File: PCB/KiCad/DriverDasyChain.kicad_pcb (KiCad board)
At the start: 4 copper layers, 66.8 x 64 mm, 52 parts, among them J1 Conn_01x03, J10 Conn_01x04, J12 Conn_01x04, J2 Conn_01x03, J3 Conn_01x03, J4 Conn_01x04, J5 Conn_01x03, J6 Conn_01x04, Q2 IRLR3410TRPBF, SW1 SW_DIP_x02, SW2 SW_SPDT, U1 AP2112K-3.3, U2 XIAO-ESP32-S3-DIP, U3 74AHCT1G125, U4 SN65HVD230

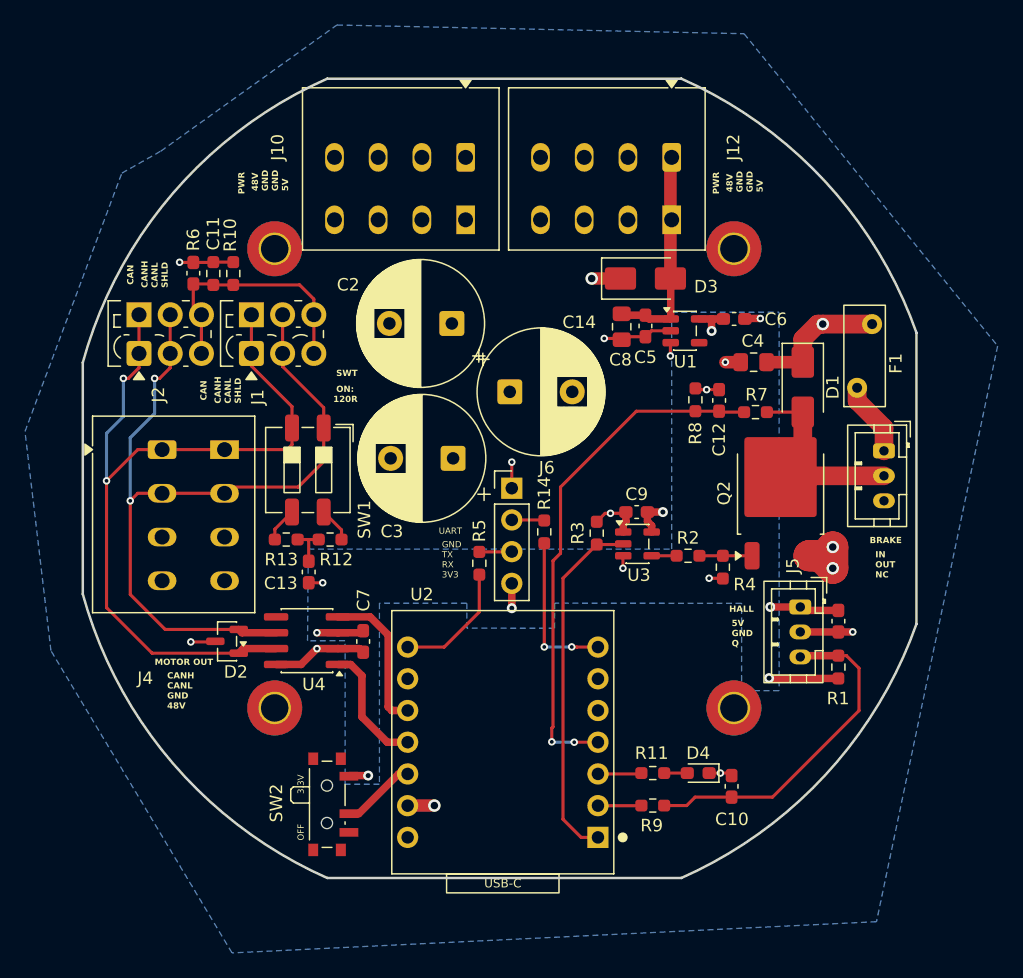
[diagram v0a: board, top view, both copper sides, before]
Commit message: Update PCB daisy chain documentation and layout details
- Enhanced power distribution details for the daisy chain, including updated capacitor specifications for bulk capacitance.
- Clarified the layout topology for the braking circuit and updated the placement of the flyback diode.
- Added a CAN-TVS protection component to the schematic and layout, ensuring proper placement for transceiver protection.
- Verified and documented layout standards, including ground and power plane considerations, and ensured compliance with IPC-2221 standards.
- Updated the status of various tasks related to the PCB design, including completion of split-termination and CAN-TVS integration.
- Added a lock file for the KiCad PCB project to track user access.
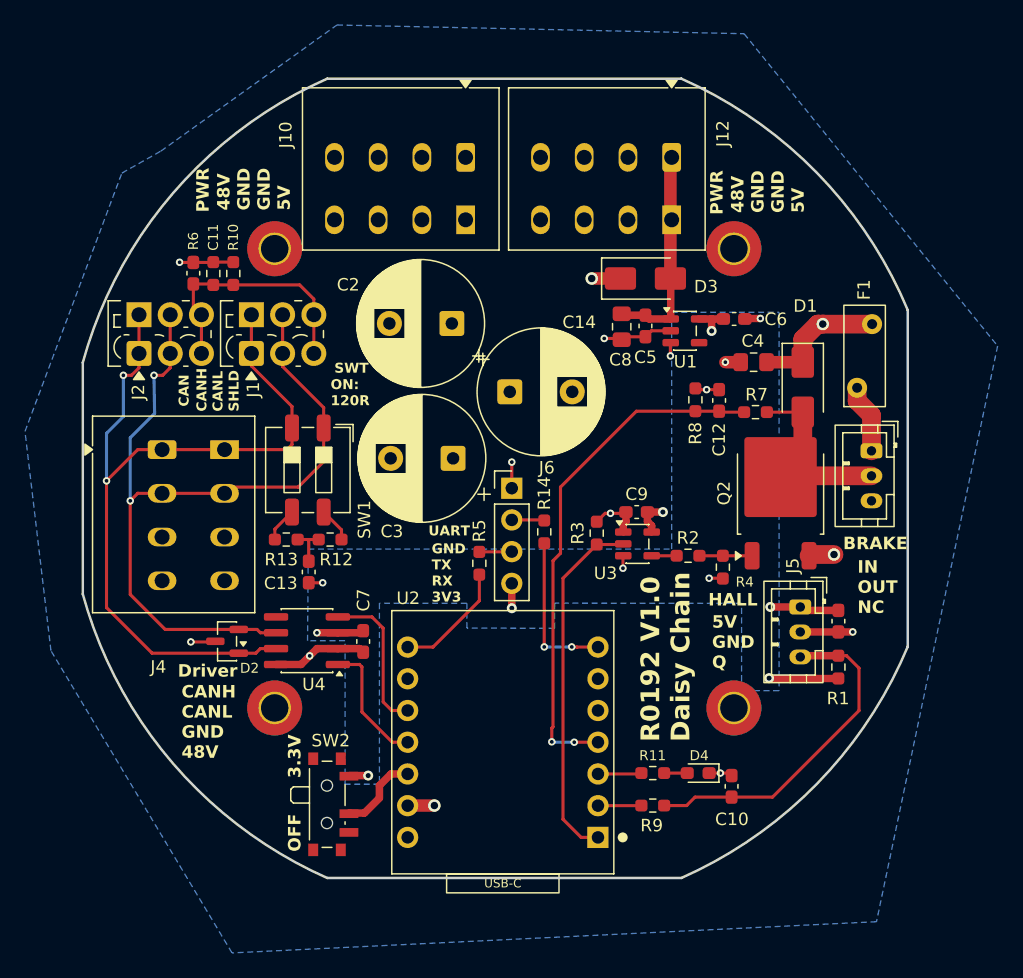
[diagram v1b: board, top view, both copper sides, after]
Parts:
- moved J3 1.00 mm to (179.4, 97.8)
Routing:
- net GND: track 51.1 -> 46.9 mm, vias 18 -> 17
- net /BRAKE Out: track 17.1 -> 16.1 mm
- net Net-(SW2-B): track 6.02 -> 6.60 mm
- net /GPIO D7 (XIAO-ESP32-S3): track 9.89 -> 9.36 mm
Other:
- board size 66.8 x 64 mm -> 66.1 x 64 mm
- board text added: "Driver"
- board text added: "R0192 V1.0 Daisy Chain"
- board text removed: "MOTOR OUT"

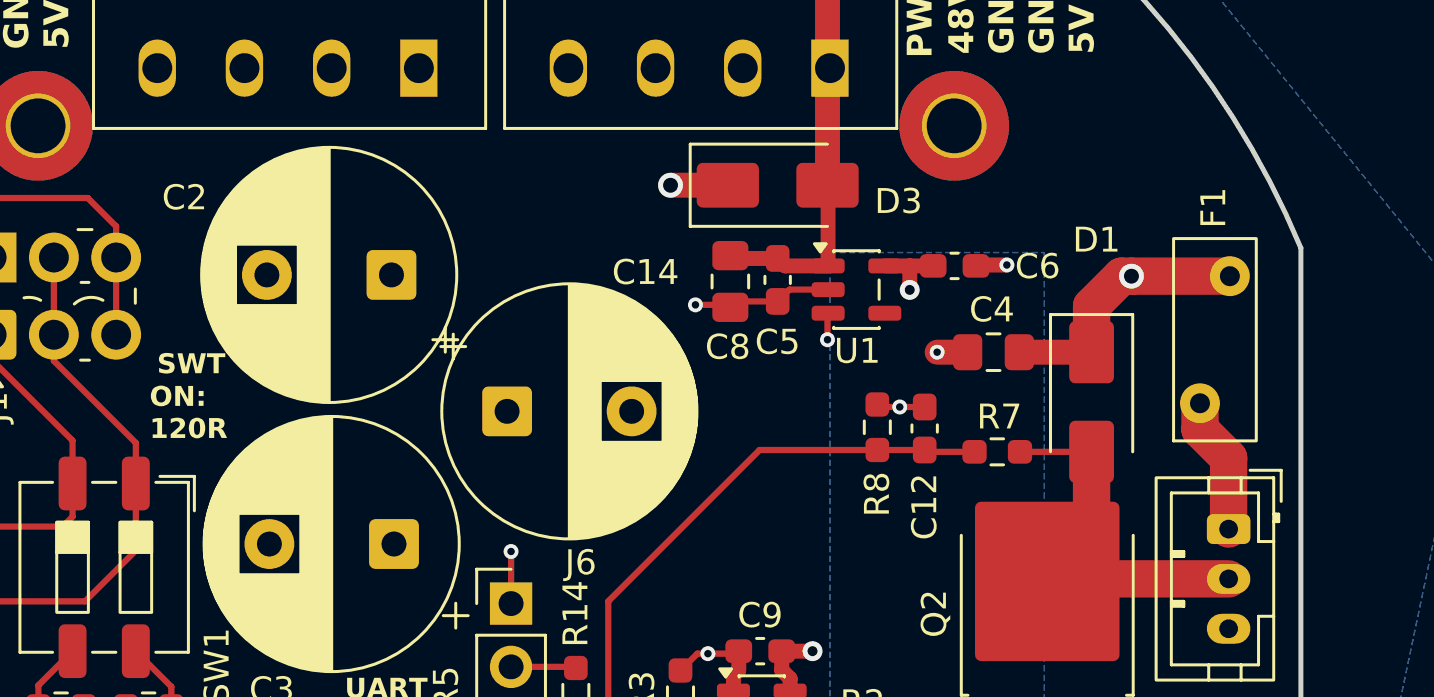
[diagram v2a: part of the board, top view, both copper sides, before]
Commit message: Add TVS diode protection and update schematic documentation
- Updated the `DriverDasyChain.kicad_pro` file to include used designators for power components.
- Added a new SMAJ58A diode symbol to the schematic (`DriverDasyChain.kicad_sch`) for transient voltage suppression, including properties and connections.
- Enhanced documentation in `pcb_daisy_chain.md` to explain the role of the new TVS diode (D5) as a protection for Q2 and its placement details.
- Clarified the rationale for using a 58V TVS diode and its implications for circuit protection.
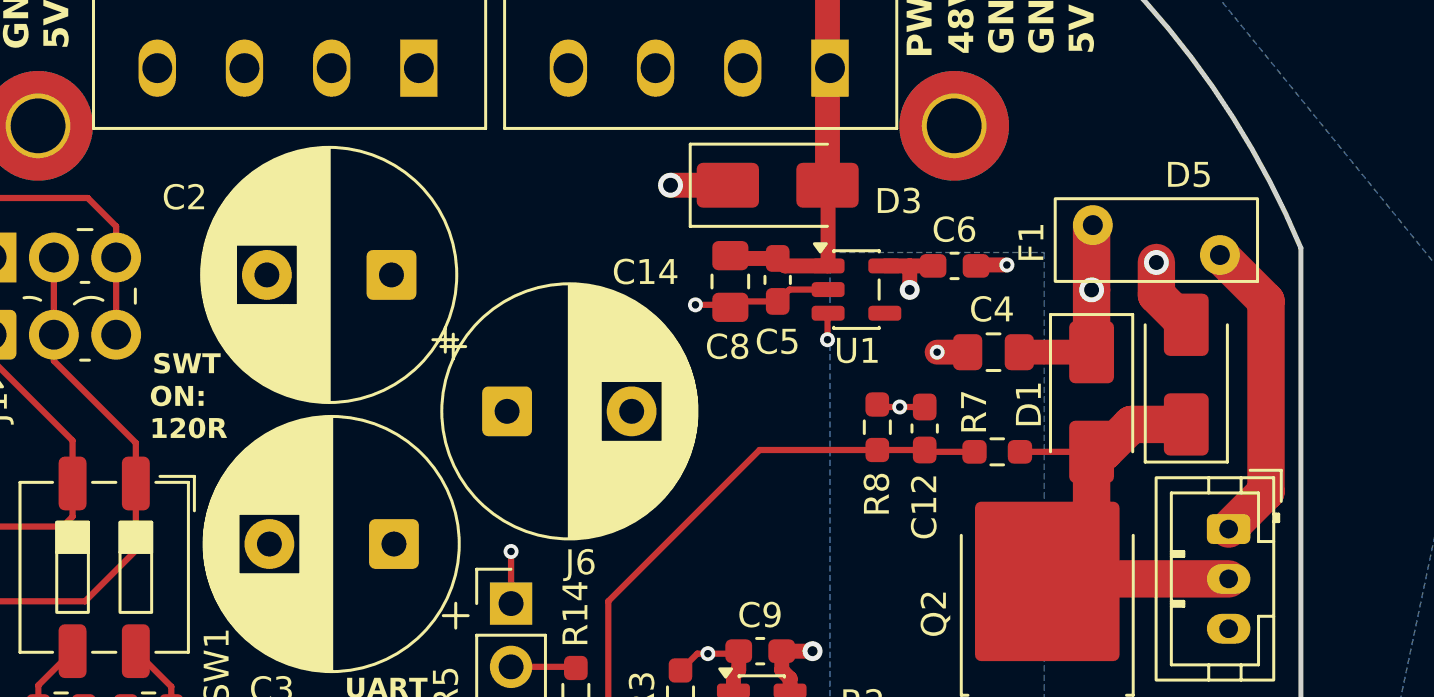
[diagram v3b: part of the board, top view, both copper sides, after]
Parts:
- added D5: SMAJ58A, Diode_SMD:D_SMA, F.Cu at (177.7, 91.6)
- D4: value LED -> LTST-C191KRKT
- moved F1 6.00 mm to (179.1, 86.8), turned to 180 degrees
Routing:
- net /BRAKE +48V: track 5.53 -> 12.4 mm
- net /BRAKE Out: track 16.1 -> 20.4 mm
- net GND: track 46.9 -> 49.9 mm, vias 17 -> 18
- net +48V: track 10.8 -> 8.02 mm
